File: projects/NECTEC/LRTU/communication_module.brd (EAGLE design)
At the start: 121.1 x 70.6 mm, 44 parts, among them Q1 BC847BS, U1 ESP-WROOM-32U (w/uFL), U2 IMAS980TH, U3 WG209_3E6, U4 RFM95W_SMT, X1 uFL, X2 uFL

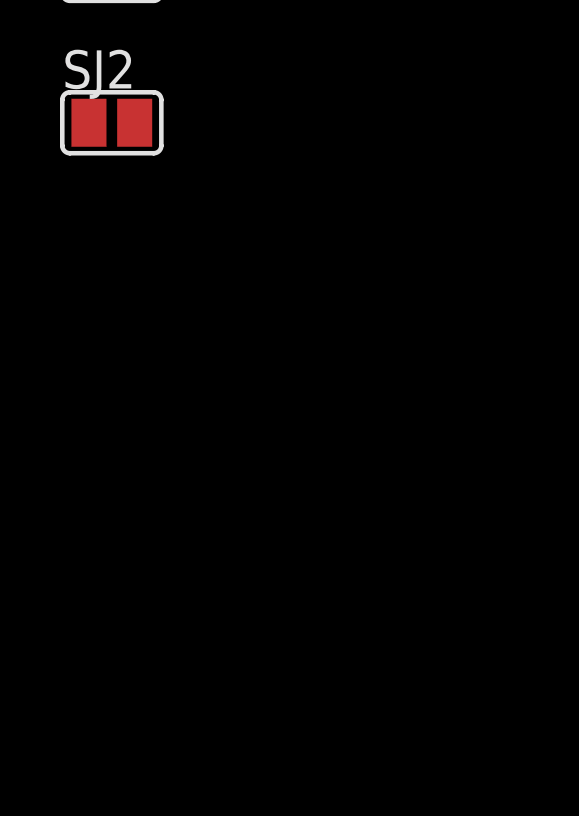
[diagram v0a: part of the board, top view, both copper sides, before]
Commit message: Fix ESP-eMOD connection, adding pull-up and swap uart pins.
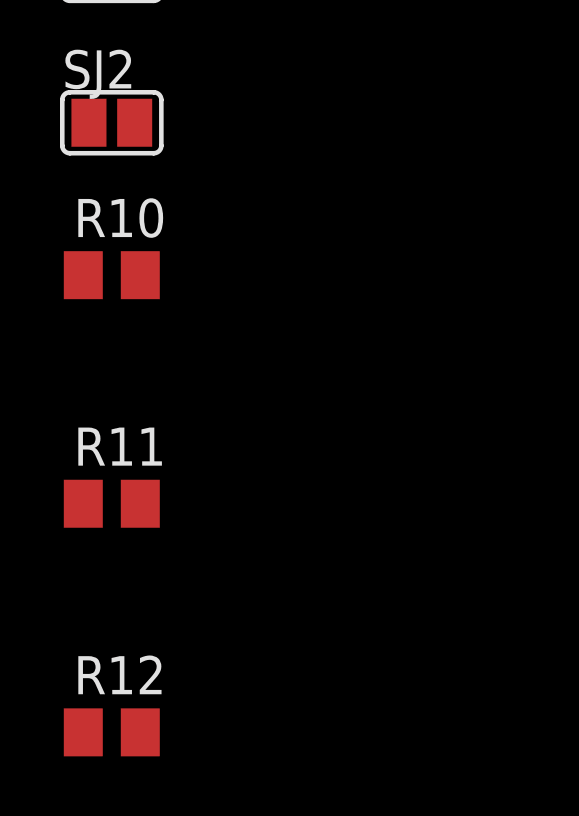
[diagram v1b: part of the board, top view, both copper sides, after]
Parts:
- added R10, R11, R12: 100k, ipas:RCL_M0805
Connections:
- net +3V3: now also R10.1, R11.2, R12.2
- net IM_INT: now also R11.1
- net IM_RXD: now also U1.26; no longer U1.6
- net IM_TXD: now also R12.1, U1.6; no longer U1.26
- net TXD_TTL0: now also R10.2
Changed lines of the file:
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@@
 <attribute name="VALUE" x="-164.211" y="-228.727" size="1.27" layer="27" ratio="10"/>
+</element>
+<element name="R10" library="ipas" package="RCL_M0805" value="100k" x="-162.56" y="-231.14" smashed="yes">
+<attribute name="NAME" x="-163.83" y="-229.87" size="1.27" layer="25"/>
+<attribute name="VALUE" x="-163.83" y="-233.68" size="1.27" layer="27"/>
+</element>
+<element name="R11" library="ipas" package="RCL_M0805" value="100k" x="-162.56" y="-238.76" smashed="yes">
+<attribute name="NAME" x="-163.83" y="-237.49" size="1.27" layer="25"/>
+<attribute name="VALUE" x="-163.83" y="-241.3" size="1.27" layer="27"/>
+</element>
+<element name="R12" library="ipas" package="RCL_M0805" value="100k" x="-162.56" y="-246.38" smashed="yes">
+<attribute name="NAME" x="-163.83" y="-245.11" size="1.27" layer="25"/>
+<attribute name="VALUE" x="-163.83" y="-248.92" size="1.27" layer="27"/>
 </element>
 </elements>
@@
 <contactref element="JP11" pad="18"/>
 <contactref element="U1" pad="27"/>
-<wire x1="99.06" y1="43.18" x2="47.858" y2="7.254" width="0" layer="19" extent="1-1"/>
+<contactref element="R10" pad="2"/>
+<wire x1="47.858" y1="7.254" x2="99.06" y2="43.18" width="0" layer="19" extent="1-1"/>
+<wire x1="-161.61" y1="-231.14" x2="47.858" y2="7.254" width="0" layer="19" extent="1-1"/>
 </signal>
 <signal name="SDA_IO_EXP">
@@
 <contactref element="U3" pad="5P"/>
 <contactref element="U3" pad="5"/>
+<contactref element="R10" pad="1"/>
+<contactref element="R11" pad="2"/>
+<contactref element="R12" pad="2"/>
 <contactref element="LED2" pad="A"/>
 <wire x1="-109.35" y1="-115.57" x2="-100.33" y2="-143.51" width="0" layer="19" extent="1-1"/>
@@
 <wire x1="-109.35" y1="-91.44" x2="-109.35" y2="-97.79" width="0" layer="19" extent="1-1"/>
 <wire x1="-99.99" y1="-82.55" x2="-109.35" y2="-91.44" width="0" layer="19" extent="1-1"/>
+<wire x1="-114.3" y1="-196.63" x2="-100.33" y2="-143.51" width="0" layer="19" extent="1-1"/>
+<wire x1="-163.51" y1="-231.14" x2="-114.3" y2="-196.63" width="0" layer="19" extent="1-1"/>
+<wire x1="-161.61" y1="-238.76" x2="-163.51" y2="-231.14" width="0" layer="19" extent="1-1"/>
+<wire x1="-161.61" y1="-246.38" x2="-161.61" y2="-238.76" width="0" layer="19" extent="1-1"/>
 <wire x1="15.0678625" y1="27.7304" x2="-99.99" y2="-82.55" width="0" layer="19" extent="1-1"/>
-<wire x1="42.25" y1="39.5" x2="-100.33" y2="-143.51" width="0" layer="19" extent="1-1"/>
-<wire x1="42.25" y1="38.7" x2="42.25" y2="39.5" width="0" layer="19" extent="1-1"/>
-<wire x1="-114.3" y1="-196.63" x2="42.25" y2="38.7" width="0" layer="19" extent="1-1"/>
-<wire x1="76.2" y1="64.77" x2="15.0678625" y2="27.7304" width="0" layer="19" extent="1-1"/>
+<wire x1="29.358" y1="19.954" x2="15.0678625" y2="27.7304" width="0" layer="19" extent="1-1"/>
+<wire x1="42.25" y1="38.7" x2="29.358" y2="19.954" width="0" layer="19" extent="1-1"/>
+<wire x1="42.25" y1="39.5" x2="42.25" y2="38.7" width="0" layer="19" extent="1-1"/>
+<wire x1="25.372" y1="50.022" x2="42.25" y2="39.5" width="0" layer="19" extent="1-1"/>
+<wire x1="5.4" y1="63.5" x2="25.372" y2="50.022" width="0" layer="19" extent="1-1"/>
+<wire x1="53.66" y1="7.62" x2="29.358" y2="19.954" width="0" layer="19" extent="1-1"/>
+<wire x1="76.2" y1="64.77" x2="42.25" y2="39.5" width="0" layer="19" extent="1-1"/>
 <wire x1="115.91" y1="62.23" x2="76.2" y2="64.77" width="0" layer="19" extent="1-1"/>
 <wire x1="101.6" y1="22.86" x2="115.91" y2="62.23" width="0" layer="19" extent="1-1"/>
-<wire x1="53.66" y1="7.62" x2="101.6" y2="22.86" width="0" layer="19" extent="1-1"/>
-<wire x1="5.4" y1="63.5" x2="53.66" y2="7.62" width="0" layer="19" extent="1-1"/>
-<wire x1="25.372" y1="50.022" x2="115.91" y2="62.23" width="0" layer="19" extent="1-1"/>
-<wire x1="29.358" y1="19.954" x2="25.372" y2="50.022" width="0" layer="19" extent="1-1"/>
 </signal>
 <signal name="+5V">
@@
 <signal name="IM_RXD">
 <contactref element="U2" pad="18"/>
-<contactref element="U1" pad="6"/>
-<wire x1="29.358" y1="14.874" x2="13.037659375" y2="27.7304" width="0" layer="19" extent="1-1"/>
+<contactref element="U1" pad="26"/>
+<wire x1="13.037659375" y1="27.7304" x2="47.858" y2="5.984" width="0" layer="19" extent="1-1"/>
 </signal>
 <signal name="IM_TXD">
 <contactref element="U2" pad="19"/>
-<contactref element="U1" pad="26"/>
-<wire x1="47.858" y1="5.984" x2="11.0268375" y2="27.735478125" width="0" layer="19" extent="1-1"/>
+<contactref element="U1" pad="6"/>
+<contactref element="R12" pad="1"/>
+<wire x1="29.358" y1="14.874" x2="-163.51" y2="-246.38" width="0" layer="19" extent="1-1"/>
+<wire x1="11.0268375" y1="27.735478125" x2="29.358" y2="14.874" width="0" layer="19" extent="1-1"/>
 </signal>
 <signal name="IM_INT">
 <contactref element="U2" pad="20"/>
 <contactref element="U1" pad="7"/>
+<contactref element="R11" pad="1"/>
+<wire x1="9.0195" y1="27.7304" x2="-163.51" y2="-238.76" width="0" layer="19" extent="1-1"/>
 <wire x1="29.358" y1="13.604" x2="9.0195" y2="27.7304" width="0" layer="19" extent="1-1"/>
 </signal>
